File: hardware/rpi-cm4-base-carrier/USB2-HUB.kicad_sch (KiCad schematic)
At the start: 32 parts, among them J10 Conn_02x05_Odd_Even, J8 USB_OTG, J9 690-008-221-904, U10 TPD4EUSB30, U11 AP22653W6, U8 FSUSB42MUX, U9 USB2514B-I/M2, Y1 24MHz

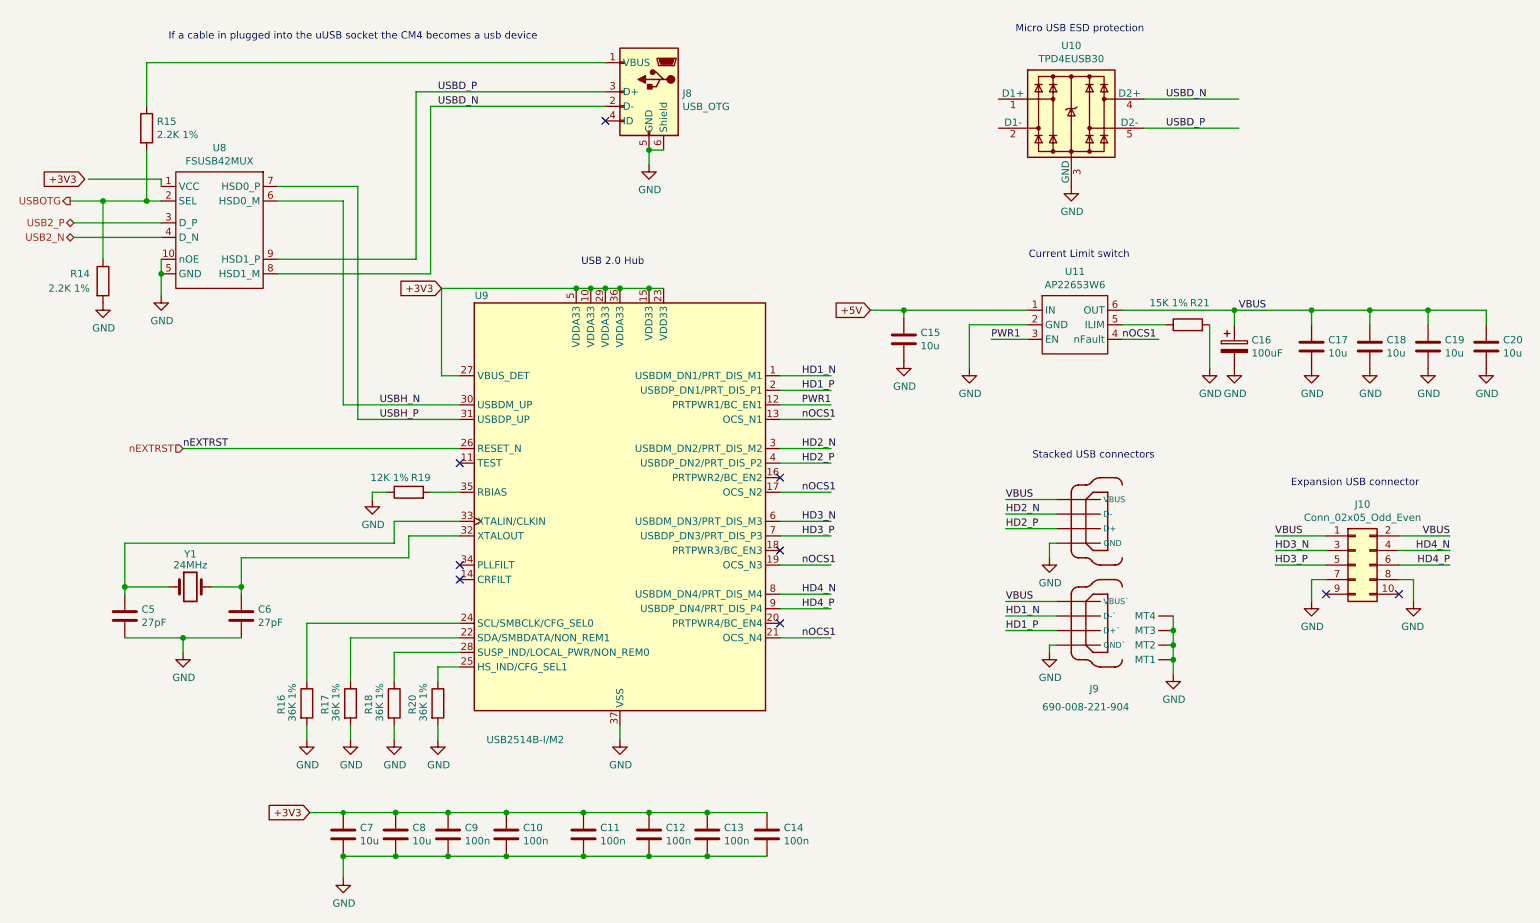
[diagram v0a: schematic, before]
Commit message: routing for some modules progressing quickly, USBHUB mostly complete, thought needed regarding which connectors should be exposed post assembly and which should be for internal use only. LED identifiers and buttons still missing
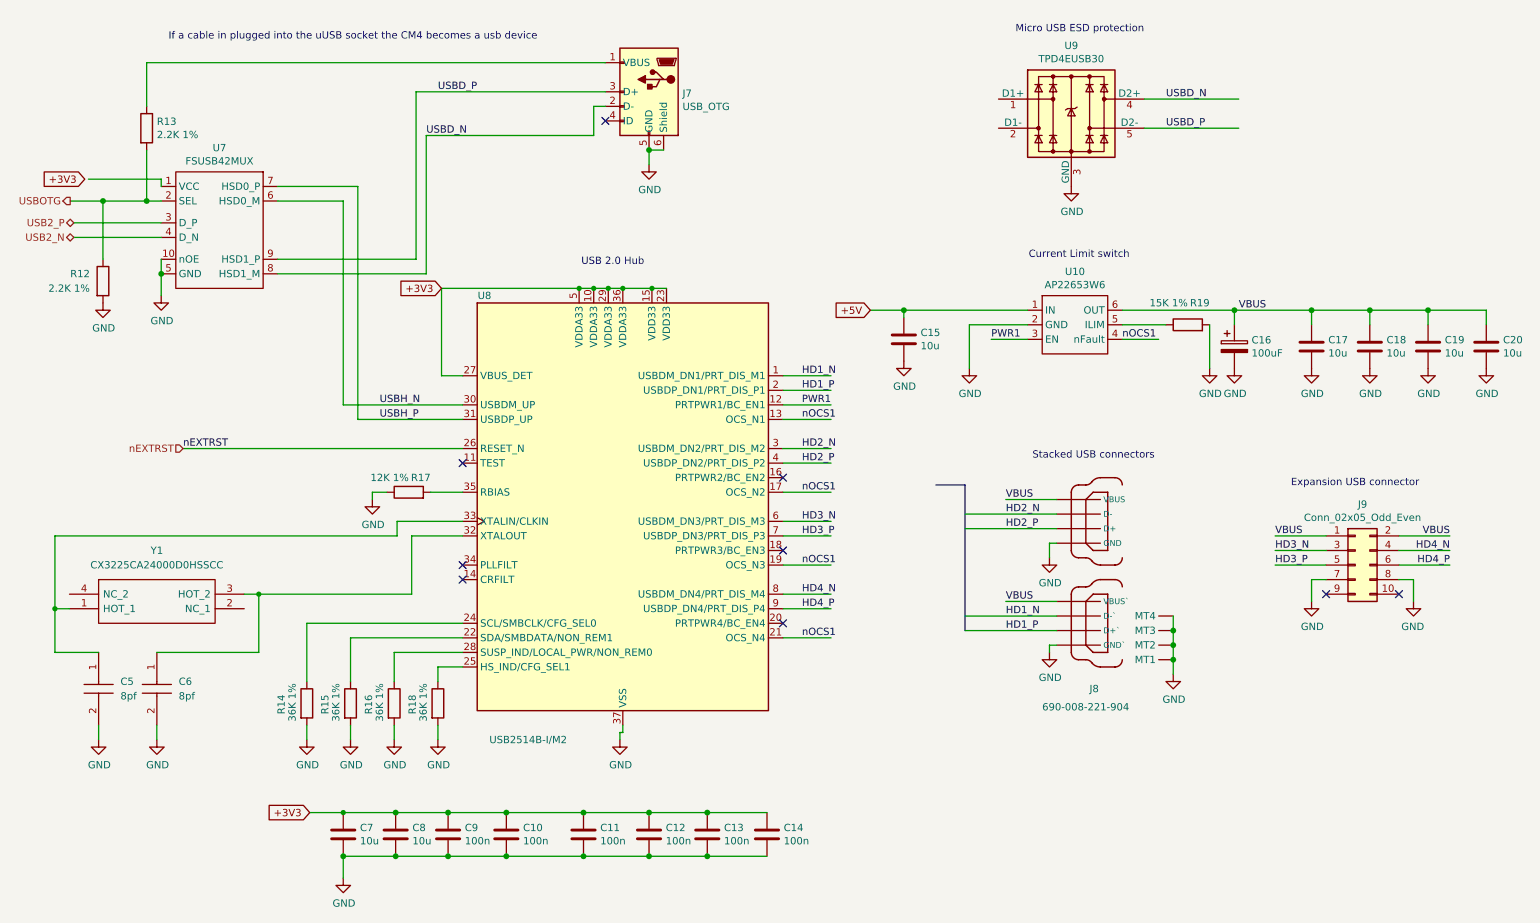
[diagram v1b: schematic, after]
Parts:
- removed C5, C6: 27pF, Capacitor_SMD:C_0402_1005Metric, symbol Device:C
- removed Y1: 24MHz, Crystal:Crystal_SMD_HC49-SD, symbol Device:Crystal
- added C5, C6: 8pf, CAPC1005X56N, symbol SamacSys_Parts:0402YA8R0DAT2A
- added Y1: CX3225CA24000D0HSSCC, CX3225CA24000D0HSSCC, symbol SamacSys_Parts:CX3225CA24000D0HSSCC
- renumbered J8 to J7, J9 to J8, J10 to J9, R14 to R12, R15 to R13, R16 to R14, R17 to R15, R18 to R16, R19 to R17, R20 to R18, R21 to R19, U11 to U10, U8 to U7, U9 to U8, U10 to U9
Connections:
- net GND: now also C5.2, C6.2
- net at U8.32 (XTALOUT): now also C6.1, Y1.3 (HOT_2)
- net at U8.33 (XTALIN/CLKIN): now also C5.1, Y1.1 (HOT_1)
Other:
- moved on the sheet: U8

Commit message: started final placement of blocks, realised ESD suppression devices cannot be manufactured with JLC, need to switch part
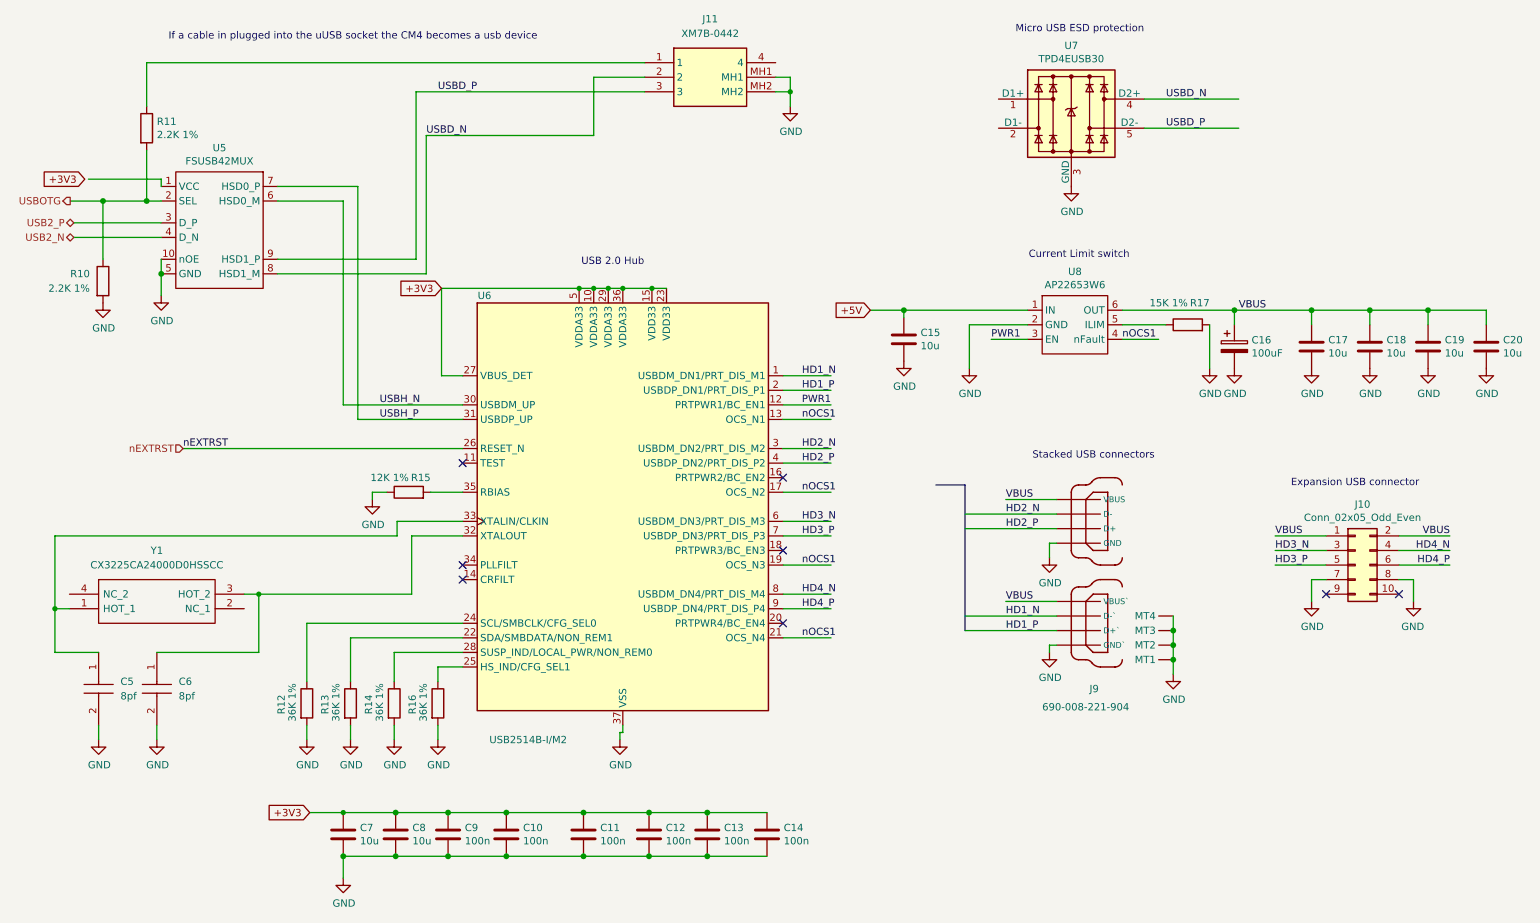
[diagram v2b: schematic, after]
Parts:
- removed J7: USB_OTG, CM4IO:USB_Micro-B_EDAC_UCON00686, symbol Connector:USB_OTG
- added J11: XM7B-0442, XM7B0442, symbol SamacSys_Parts:XM7B-0442
- C5, C6: footprint CAPC1005X56N -> SamacSys_Parts:CAPC1005X56N
- Y1: footprint CX3225CA24000D0HSSCC -> SamacSys_Parts:CX3225CA24000D0HSSCC
- renumbered J9 to J10, J8 to J9, R12 to R10, R13 to R11, R14 to R12, R15 to R13, R16 to R14, R17 to R15, R18 to R16, R19 to R17, U7 to U5, U8 to U6, U9 to U7, U10 to U8
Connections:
- net GND: now also J11.MH1, J11.MH2
- net USBD_N: now also J11.2
- net USBD_P: now also J11.3
- net at R11.1: now also J11.1
- no-connect marks 9 -> 8

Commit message: started to route core connectors to CM4, RJ45 annoyingly has the inverse pinout to CM4, need to work out how to uncross tracking sensibly
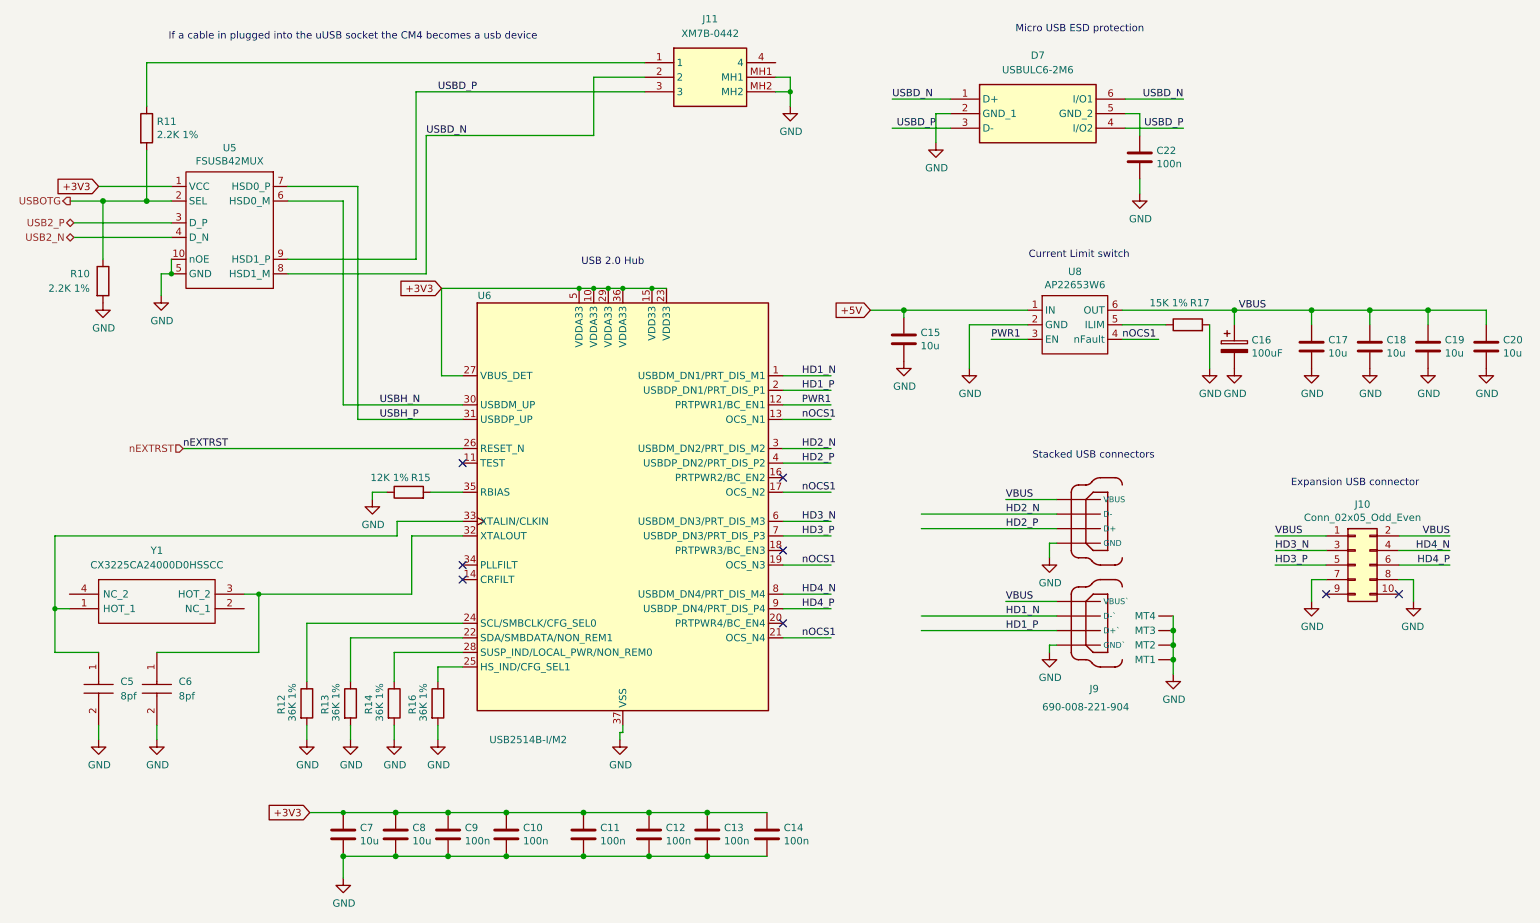
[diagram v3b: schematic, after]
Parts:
- removed U7: TPD4EUSB30, Package_SON:USON-10_2.5x1.0mm_P0.5mm, symbol CM4IO:TPD4EUSB30
- added C22: 100n, Capacitor_SMD:C_0402_1005Metric, symbol Device:C
- added D7: USBULC6-2M6, SON50P100X145X60-6N-D, symbol SamacSys_Parts:USBULC6-2M6
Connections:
- net USBD_P is gone; now on net GND: J11.3, U5.9 (HSD1_P)
- net +3V3: now also U5.1 (VCC)
- net GND: now also C22.2, D7.2 (GND_1), D7.3 (D-), D7.4 (I/O2)
- net USBD_N: now also D7.1 (D+), D7.6 (I/O1)
- new net: C22.1, D7.5 (GND_2)
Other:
- moved on the sheet: U5

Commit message: schematic entry for samtec board edge connector complete, started breakout of GPIO lines for connection to board edge connector
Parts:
- D7: footprint SON50P100X145X60-6N-D -> SamacSys_Parts:SON50P100X145X60-6N-D
- J11: footprint XM7B0442 -> SamacSys_Parts:XM7B0442
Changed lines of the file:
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@@
       (effects (font (size 1.27 1.27)))
     )
-    (property "Footprint" "XM7B0442" (at 144.78 126.67 0)
+    (property "Footprint" "SamacSys_Parts:XM7B0442" (at 144.78 126.67 0)
       (effects (font (size 1.27 1.27)) (justify left top) hide)
     )
@@
       (effects (font (size 1.27 1.27)))
     )
-    (property "Footprint" "SON50P100X145X60-6N-D" (at 205.74 133.02 0)
+    (property "Footprint" "SamacSys_Parts:SON50P100X145X60-6N-D" (at 205.74 133.02 0)
       (effects (font (size 1.27 1.27)) (justify left top) hide)
     )

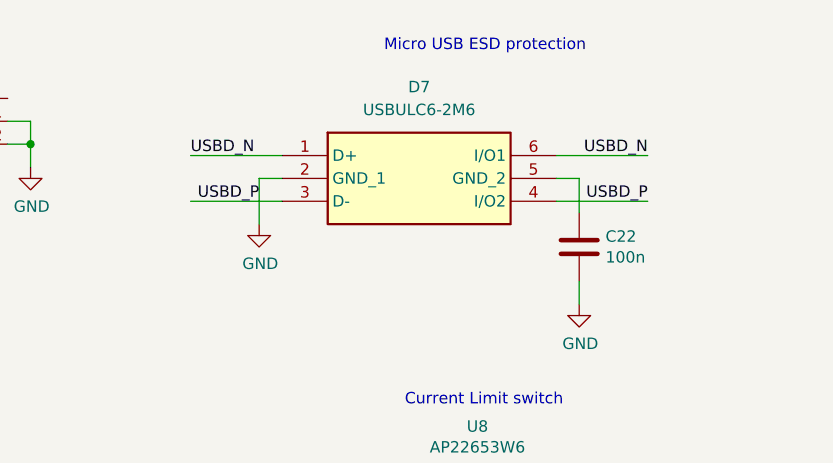
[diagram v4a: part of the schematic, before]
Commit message: fan control added to sch, layout 90% complete, awaiting review
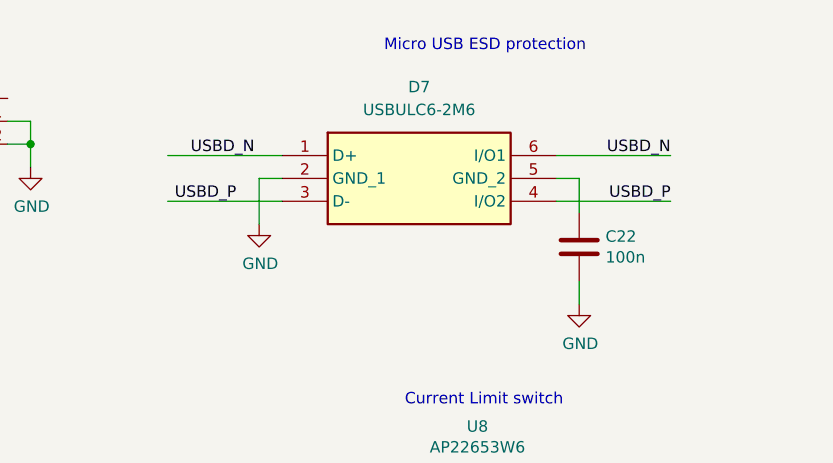
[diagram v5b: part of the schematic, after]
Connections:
- net GND: no longer D7.3 (D-), D7.4 (I/O2), J11.3, U5.9 (HSD1_P)
- new net USBD_P: D7.3 (D-), D7.4 (I/O2), J11.3, U5.9 (HSD1_P)
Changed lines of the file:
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@@
     (stroke (width 0) (type solid))
-  )
-  (wire (pts (xy 209.55 43.18) (xy 219.71 43.18))
-    (stroke (width 0) (type default))
   )
   (wire (pts (xy 242.062 77.47) (xy 242.062 74.93))
@@
     (stroke (width 0) (type solid))
   )
-  (wire (pts (xy 209.55 38.1) (xy 219.71 38.1))
-    (stroke (width 0) (type default))
-  )
   (wire (pts (xy 25.4 127) (xy 22.86 127))
     (stroke (width 0) (type default))
@@
     (stroke (width 0) (type solid))
   )
-  (wire (pts (xy 168.91 38.1) (xy 179.07 38.1))
+  (wire (pts (xy 166.37 38.1) (xy 179.07 38.1))
     (stroke (width 0) (type default))
   )
@@
     (stroke (width 0) (type solid))
   )
+  (wire (pts (xy 209.55 43.18) (xy 222.25 43.18))
+    (stroke (width 0) (type default))
+  )
   (wire (pts (xy 91.44 170.18) (xy 101.6 170.18))
     (stroke (width 0) (type solid))
@@
     (stroke (width 0) (type solid))
   )
-  (wire (pts (xy 168.91 43.18) (xy 179.07 43.18))
-    (stroke (width 0) (type default))
-  )
   (wire (pts (xy 85.852 36.83) (xy 125.73 36.83))
     (stroke (width 0) (type solid))
   )
+  (wire (pts (xy 209.55 38.1) (xy 222.25 38.1))
+    (stroke (width 0) (type default))
+  )
   (wire (pts (xy 165.1 74.93) (xy 170.942 74.93))
     (stroke (width 0) (type solid))
@@
     (stroke (width 0) (type solid))
   )
-  (wire (pts (xy 176.53 45.72) (xy 176.53 40.64))
+  (wire (pts (xy 176.53 40.64) (xy 176.53 45.72))
     (stroke (width 0) (type default))
   )
@@
   (wire (pts (xy 88.392 106.68) (xy 93.98 106.68))
     (stroke (width 0) (type solid))
+  )
+  (wire (pts (xy 166.37 43.18) (xy 179.07 43.18))
+    (stroke (width 0) (type default))
   )
   (wire (pts (xy 63.5 53.34) (xy 75.692 53.34))
@@
     (effects (font (size 1.27 1.27)) (justify left bottom))
   )
-  (label "USBD_N" (at 219.71 38.1 180) (fields_autoplaced)
+  (label "USBD_N" (at 222.25 38.1 180) (fields_autoplaced)
     (effects (font (size 1.27 1.27)) (justify right bottom))
   )
@@
     (effects (font (size 1.27 1.27)) (justify right bottom))
   )
-  (label "USBD_P" (at 219.71 43.18 180) (fields_autoplaced)
+  (label "USBD_P" (at 222.25 43.18 180) (fields_autoplaced)
     (effects (font (size 1.27 1.27)) (justify right bottom))
   )
@@
     (effects (font (size 1.27 1.27)) (justify left bottom))
   )
-  (label "USBD_P" (at 176.53 43.18 180) (fields_autoplaced)
-    (effects (font (size 1.27 1.27)) (justify right bottom))
-  )
+  (label "USBD_P" (at 173.99 43.18 180) (fields_autoplaced)
+    (effects (font (size 1.27 1.27)) (justify right bottom))
+  )
